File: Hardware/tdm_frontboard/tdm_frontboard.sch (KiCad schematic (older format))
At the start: 90 parts, among them J1 Conn_02x06_Counter_Clockwise, J2 0.96_OLED, SW1 SW_SPST, SW10 SW_SPST, SW11 SW_SPST, SW12 SW_SPST, SW13 SW_SPST, SW14 SW_SPST, SW15 SW_SPST, SW16 SW_SPST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

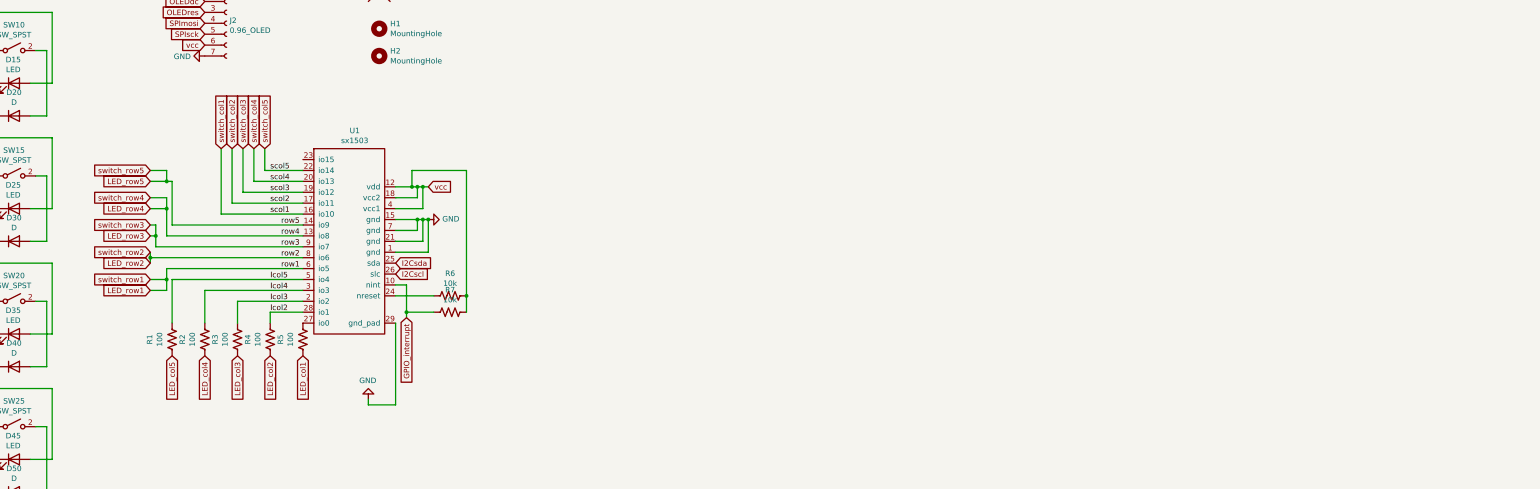
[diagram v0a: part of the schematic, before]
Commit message: playing around with samd11 for the frontboard, reworked power on the back
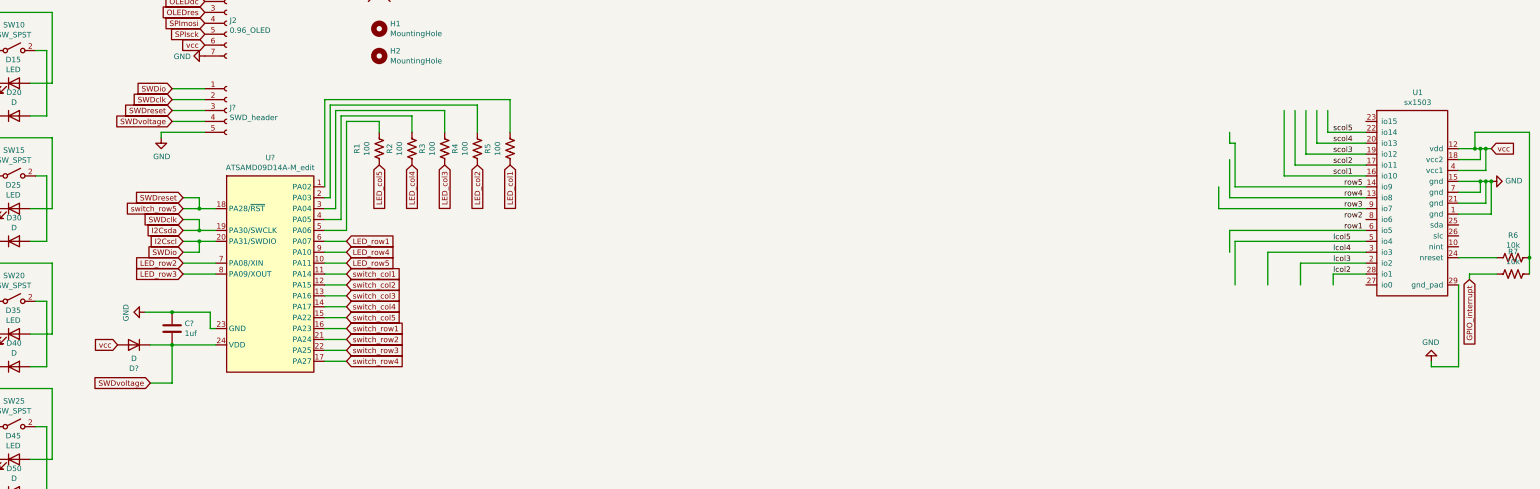
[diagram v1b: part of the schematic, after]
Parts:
- added C?: 1uf, symbol Device:C
- added D?: D, custom:Diode_0603_HandSoldering, symbol Device:D
- added J?: SWD_header, symbol Connector:Conn_01x05_Female
- added U?: ATSAMD09D14A-M_edit, Package_DFN_QFN:QFN-24-1EP_4x4mm_P0.5mm_EP2.6x2.6mm, symbol customLibrary:ATSAMD09D14A-M_edit
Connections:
- net labels added: SWDclk, SWDio, SWDreset, SWDvoltage
- wire segments 397 -> 440
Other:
- moved on the sheet: R1, R2, R3, R4, R5, R6, R7, U1
